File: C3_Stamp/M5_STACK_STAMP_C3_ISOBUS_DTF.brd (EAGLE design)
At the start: 53.3 x 30.5 mm, 13 parts, among them IC1 MCP2562-E_P, J1 61300811121, J2 61300611121, J3 DTF13-4P

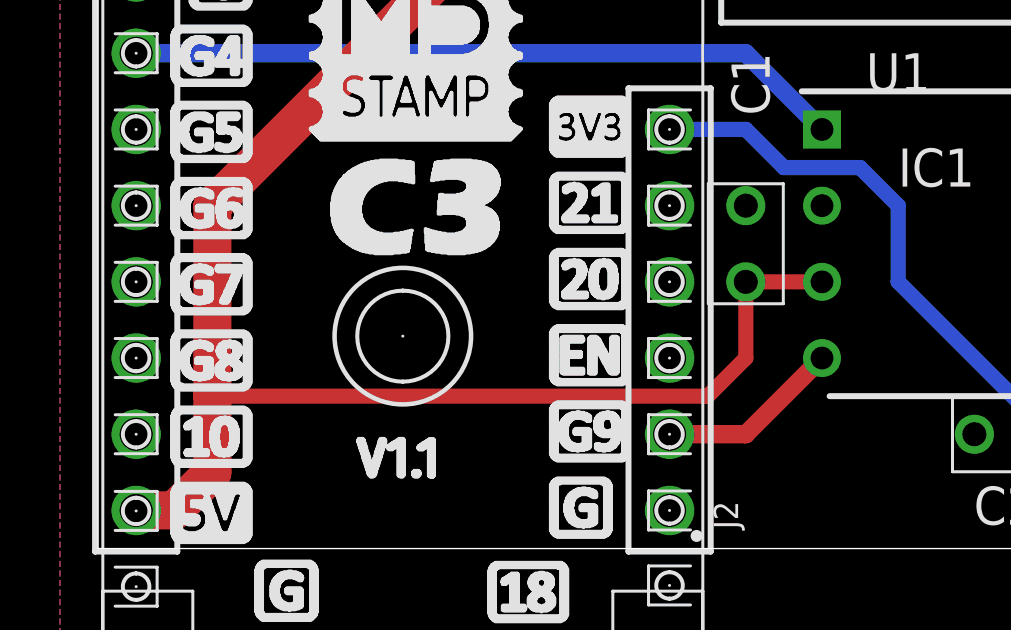
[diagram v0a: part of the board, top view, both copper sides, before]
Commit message: G7 for CAN RX, as G9 is a Strapping Pin.
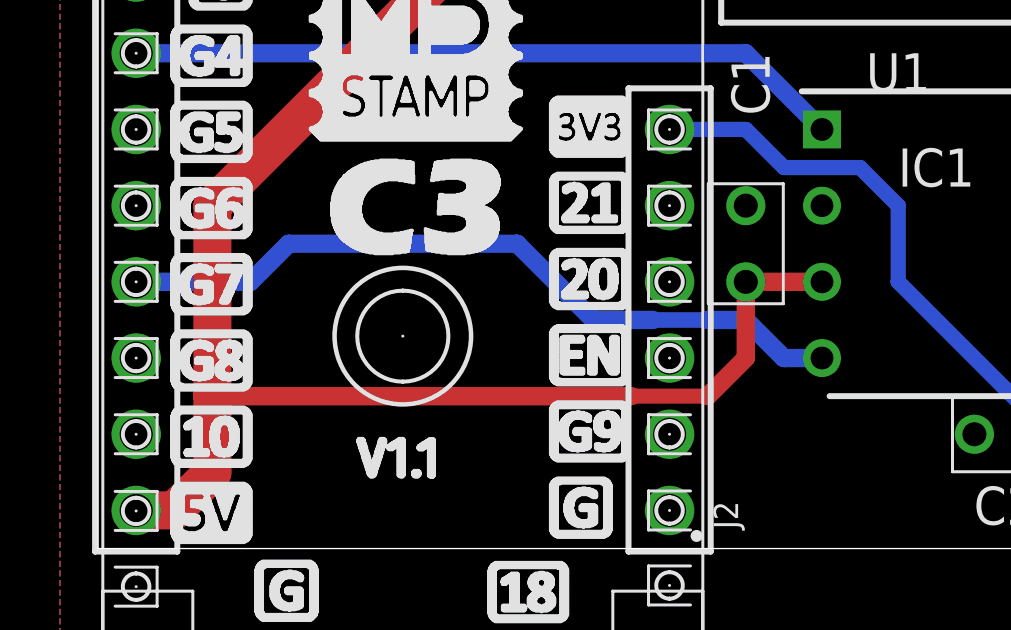
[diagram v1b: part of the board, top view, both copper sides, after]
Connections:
- net G7: now also IC1.4
- net G9: no longer IC1.4
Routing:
- net G7: track 0.00 -> 25.0 mm
- net G9: track 6.13 -> 0.00 mm
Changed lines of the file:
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@@
 <contactref element="IC1" pad="3"/>
 <wire x1="20.32" y1="25.4" x2="25.4" y2="25.4" width="1.27" layer="1"/>
-<wire x1="22.86" y1="10.16" x2="25.4" y2="10.16" width="0.508" layer="1"/>
-<wire x1="22.86" y1="10.16" x2="22.86" y2="7.62" width="0.508" layer="1"/>
-<wire x1="22.86" y1="7.62" x2="21.59" y2="6.35" width="0.508" layer="1"/>
-<wire x1="21.59" y1="6.35" x2="5.08" y2="6.35" width="0.508" layer="1"/>
+<wire x1="22.86" y1="10.16" x2="25.4" y2="10.16" width="0.6096" layer="1"/>
+<wire x1="22.86" y1="10.16" x2="22.86" y2="7.62" width="0.6096" layer="1"/>
+<wire x1="21.59" y1="6.35" x2="22.86" y2="7.62" width="0.6096" layer="1"/>
 <wire x1="2.54" y1="2.54" x2="3.81" y2="2.54" width="1.27" layer="1"/>
 <wire x1="3.81" y1="2.54" x2="5.08" y2="3.81" width="1.27" layer="1"/>
 <wire x1="5.08" y1="3.81" x2="5.08" y2="6.35" width="1.27" layer="1"/>
-<wire x1="5.08" y1="6.35" x2="5.08" y2="12.7" width="1.27" layer="1"/>
+<wire x1="5.08" y1="12.7" x2="5.08" y2="6.35" width="1.27" layer="1"/>
 <wire x1="5.08" y1="12.7" x2="17.78" y2="25.4" width="1.27" layer="1"/>
 <wire x1="17.78" y1="25.4" x2="20.32" y2="25.4" width="1.27" layer="1"/>
+<wire x1="5.08" y1="6.35" x2="19.05" y2="6.35" width="0.6096" layer="1"/>
+<wire x1="19.05" y1="6.35" x2="21.59" y2="6.35" width="0.508" layer="1"/>
 </signal>
 <signal name="+3V3">
@@
 <signal name="G9">
 <contactref element="J2" pad="2"/>
-<contactref element="IC1" pad="4"/>
-<wire x1="20.32" y1="5.08" x2="22.86" y2="5.08" width="0.6096" layer="1"/>
-<wire x1="22.86" y1="5.08" x2="25.4" y2="7.62" width="0.6096" layer="1"/>
 </signal>
 <signal name="EN">
@@
 <signal name="G7">
 <contactref element="J1" pad="5"/>
+<contactref element="IC1" pad="4"/>
+<wire x1="2.54" y1="10.16" x2="6.35" y2="10.16" width="0.6096" layer="16"/>
+<wire x1="6.35" y1="10.16" x2="7.62" y2="11.43" width="0.6096" layer="16"/>
+<wire x1="7.62" y1="11.43" x2="15.24" y2="11.43" width="0.6096" layer="16"/>
+<wire x1="17.78" y1="8.89" x2="19.77669375" y2="8.89" width="0.6096" layer="16"/>
+<wire x1="15.24" y1="11.43" x2="17.78" y2="8.89" width="0.6096" layer="16"/>
+<wire x1="25.4" y1="7.62" x2="24.13" y2="7.62" width="0.6096" layer="16"/>
+<wire x1="24.13" y1="7.62" x2="22.86" y2="8.89" width="0.6096" layer="16"/>
+<wire x1="21.59" y1="8.89" x2="22.86" y2="8.89" width="0.6096" layer="16"/>
+<wire x1="19.77669375" y1="8.89" x2="21.59" y2="8.89" width="0.508" layer="16"/>
 </signal>
 <signal name="G6">
